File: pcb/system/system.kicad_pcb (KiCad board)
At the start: 2 copper layers, 32 parts, among them J1 Raspberry_Pi_4_GPIO, J2 Screw_Terminal_01x02, J3 Servo_1_Header, J4 Servo_2_Header, J5 Screw_Terminal_01x02, J6 Screw_Terminal_01x02, Q1 BS107A, Q2 BS107A, Q3 BS107A, Q4 BS107A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

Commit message: copium
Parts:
- added J7: Screw_Terminal_01x02, TerminalBlock_4Ucon:TerminalBlock_4Ucon_1x02_P3.50mm_Vertical, F.Cu at (169.8, 40.6)
- J1: moved to B.Cu
- Q5, Q6: footprint Package_TO_SOT_THT:TO-92L_Inline -> Package_TO_SOT_THT:TO-92L_HandSolder
- SW1: footprint Button_Switch_SMD:SW_DIP_SPSTx01_Slide_6.7x4.1mm_W6.73mm_P2.54mm_LowProfile_JPin -> Button_Switch_THT:SW_CuK_JS202011CQN_DPDT_Straight
- SW2: footprint Button_Switch_THT:SW_PUSH_6mm -> Button_Switch_THT:SW_PUSH_6mm_H4.3mm
- Sol1, Sol2, Sol3, Sol4: footprint Connector_PinSocket_2.54mm:PinSocket_1x03_P2.54mm_Vertical -> Connector_PinSocket_2.54mm:PinSocket_1x02_P2.54mm_Vertical
- moved SW2 144.0 mm to (232.1, 104.3), turned to 180 degrees
- moved Q2 103.5 mm to (189.3, 139.1), turned to 180 degrees
- moved Sol1 93.1 mm to (187.1, 125.5), turned to 180 degrees
- moved Q4 88.2 mm to (163.0, 139.2), turned to 180 degrees
- moved Sol2 83.5 mm to (169.9, 125.4), turned to 180 degrees
- moved Sol3 82.1 mm to (160.8, 125.3), turned to 180 degrees
- moved Q3 77.8 mm to (172.1, 139.2), turned to 180 degrees
- moved Sol4 77.2 mm to (178.8, 125.4), turned to 180 degrees
- moved R5 74.6 mm to (188.8, 50.0), turned to -90 degrees
- moved SW1 73.1 mm to (150.7, 72.8)
- moved D1 72.5 mm to (199.3, 55.4), turned to 90 degrees
- moved J2 70.9 mm to (227.0, 130.2), turned to 180 degrees
- moved D2 70.8 mm to (203.8, 55.4), turned to 90 degrees
- moved R7 66.1 mm to (184.8, 49.8), turned to -90 degrees
- moved J1 63.7 mm to (131.8, 55.2), turned to 180 degrees
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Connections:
- D1 pad 1: Net-(R1-Pad2) -> Net-(D1-Pad1)
- D2 pad 1: Net-(R2-Pad2) -> Net-(D2-Pad1)
- J1 pad 14: /Ground -> GND
- J1 pad 20: /Ground -> GND
- J1 pad 25: /Ground -> GND
- J1 pad 30: /Ground -> GND
- J1 pad 34: /Ground -> GND
- J1 pad 39: /Ground -> GND
- J1 pad 6: /Ground -> GND
- J1 pad 9: /Ground -> GND
- J2 pad 1: /Encoder_1_A -> /Encoder_1_B
- J2 pad 2: /Encoder_1_B -> /Encoder_1_A
- R1 pad 2: Net-(R1-Pad2) -> Net-(D1-Pad1)
- R2 pad 2: Net-(R2-Pad2) -> Net-(D2-Pad1)
- R3 pad 2: Net-(R1-Pad2) -> Net-(D1-Pad1)
- R4 pad 2: Net-(R2-Pad2) -> Net-(D2-Pad1)
- Reg1 pad 4: /Ground -> GND
- SW2 pad 1: Net-(R1-Pad1) -> Net-(U1-Pad13)
- U1 pad 13: unconnected-(U1-Pad13) -> Net-(U1-Pad13)
- U1 pad 22: Net-(R2-Pad2) -> unconnected-(U1-Pad22)
- U1 pad 23: Net-(R1-Pad2) -> unconnected-(U1-Pad23)
- U1 pad 7: unconnected-(U1-Pad7) -> Net-(D1-Pad1)
- U1 pad 8: unconnected-(U1-Pad8) -> Net-(D2-Pad1)
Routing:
- net GND: track 0.00 -> 336.4 mm
- net +8V: track 0.00 -> 173.2 mm
- net Net-(R1-Pad1): track 165.4 -> 57.0 mm
- net /GPIO_5: track 0.00 -> 107.0 mm
- net /GPIO_26: track 0.00 -> 106.8 mm
- net /GPIO_6: track 0.00 -> 105.1 mm
- net /GPIO_19: track 0.00 -> 104.7 mm
- net /3.3V: track 0.00 -> 61.8 mm
- net /Encoder_1_A: track 14.1 -> 75.8 mm
- net /Encoder_1_B: track 14.5 -> 70.7 mm
- net /Encoder_2_A: track 11.2 -> 65.5 mm
- net Net-(D1-Pad1): track 0.00 -> 52.2 mm
- net Net-(Q5-Pad1): track 0.00 -> 52.1 mm
- net /Encoder_2_B: track 11.2 -> 59.0 mm
- net /GPIO_13: track 0.00 -> 45.4 mm
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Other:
- board outline added: 142.4 x 129.3 mm

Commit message: still need to future proof pcb
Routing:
- net GND: track 336.4 -> 460.6 mm
- net Net-(R1-Pad1): track 57.0 -> 59.3 mm
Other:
- board size 142.4 x 129.3 mm -> 136.7 x 117.6 mm
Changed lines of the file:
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@@
       (xy 170.986486 44.081081)
     ) (layer "B.Cu") (width 0.2) (fill solid))
-  (gr_rect (start 105.7 34.9) (end 248.1 164.2) (layer "Edge.Cuts") (width 0.1) (fill none))
+  (gr_rect (start 112.9 34.3) (end 249.6 151.9) (layer "Edge.Cuts") (width 0.1) (fill none))
   (segment (start 147.7 99) (end 147.7 108.1) (width 1.3) (layer "F.Cu") (net 1))
   (segment (start 167.64 98) (end 168.58 98) (width 1.3) (layer "F.Cu") (net 1))
   (segment (start 168.66 57.44) (end 168.66 97.92) (width 1.3) (layer "F.Cu") (net 1))
   (segment (start 155.9225 98) (end 167.64 98) (width 1.3) (layer "F.Cu") (net 1))
+  (segment (start 193.3 141) (end 193.3 122) (width 0.5) (layer "F.Cu") (net 1))
   (segment (start 173.905 40.645) (end 174.5 41.24) (width 1.3) (layer "F.Cu") (net 1))
   (segment (start 156.5 99) (end 147.7 99) (width 1.3) (layer "F.Cu") (net 1))
@@
   (segment (start 149.0325 109.4325) (end 149.0325 109.4675) (width 1.3) (layer "F.Cu") (net 1))
   (segment (start 168.66 97.92) (end 168.58 98) (width 1.3) (layer "F.Cu") (net 1))
+  (segment (start 186.76 139.05) (end 186.76 140.76) (width 0.5) (layer "F.Cu") (net 1))
+  (segment (start 193.3 122) (end 169.4 98.1) (width 0.5) (layer "F.Cu") (net 1))
   (segment (start 174.5 41.24) (end 174.5 51.6) (width 1.3) (layer "F.Cu") (net 1))
-  (segment (start 152.725 54.83) (end 163.07 54.83) (width 0.5) (layer "F.Cu") (net 1))
+  (segment (start 152.725 54.83) (end 163.07 54.83) (width 0.7) (layer "F.Cu") (net 1))
+  (segment (start 186.76 140.76) (end 188.9 142.9) (width 0.5) (layer "F.Cu") (net 1))
   (segment (start 167.5 56.92) (end 167.5 97.86) (width 1.3) (layer "F.Cu") (net 1))
   (segment (start 156.3 98.8) (end 156.5 99) (width 1.3) (layer "F.Cu") (net 1))
+  (segment (start 175.3 51.8) (end 175.3 41.4) (width 0.5) (layer "F.Cu") (net 1))
+  (segment (start 169.4 57.7) (end 175.3 51.8) (width 0.5) (layer "F.Cu") (net 1))
   (segment (start 167.58 99) (end 168.58 98) (width 1.3) (layer "F.Cu") (net 1))
   (segment (start 149.0325 109.4675) (end 151.19 109.4675) (width 1.3) (layer "F.Cu") (net 1))
@@
   (segment (start 167.5 97.86) (end 167.64 98) (width 1.3) (layer "F.Cu") (net 1))
   (segment (start 199.272 47.764) (end 203.772 47.764) (width 0.5) (layer "F.Cu") (net 1))
+  (segment (start 169.4 98.1) (end 169.4 57.7) (width 0.5) (layer "F.Cu") (net 1))
   (segment (start 173.25 40.645) (end 173.905 40.645) (width 1.3) (layer "F.Cu") (net 1))
-  (segment (start 163.07 54.83) (end 173.25 44.65) (width 0.5) (layer "F.Cu") (net 1))
+  (segment (start 163.07 54.83) (end 173.25 44.65) (width 0.7) (layer "F.Cu") (net 1))
+  (segment (start 174.545 40.645) (end 173.25 40.645) (width 0.5) (layer "F.Cu") (net 1))
+  (segment (start 188.9 142.9) (end 191.4 142.9) (width 0.5) (layer "F.Cu") (net 1))
   (segment (start 147.7 108.1) (end 149.0325 109.4325) (width 1.3) (layer "F.Cu") (net 1))
+  (segment (start 175.3 41.4) (end 174.545 40.645) (width 0.5) (layer "F.Cu") (net 1))
   (segment (start 172.062 66.074) (end 172.062 70.574) (width 0.5) (layer "F.Cu") (net 1))
   (segment (start 173.25 40.645) (end 173.25 43.25) (width 1.3) (layer "F.Cu") (net 1))
   (segment (start 173.25 43.25) (end 173.25 51.17) (width 1.3) (layer "F.Cu") (net 1))
   (segment (start 173.25 51.17) (end 167.5 56.92) (width 1.3) (layer "F.Cu") (net 1))
+  (segment (start 191.4 142.9) (end 193.3 141) (width 0.5) (layer "F.Cu") (net 1))
   (segment (start 156.5 99) (end 167.58 99) (width 1.3) (layer "F.Cu") (net 1))
   (segment (start 174.5 51.6) (end 168.66 57.44) (width 1.3) (layer "F.Cu") (net 1))
@@
   (segment (start 169.56 139.2) (end 169.56 142.94) (width 0.5) (layer "B.Cu") (net 1))
   (segment (start 178.36 143.04) (end 178.3 143.1) (width 0.5) (layer "B.Cu") (net 1))
-  (segment (start 152.725 57.37) (end 144.33 57.37) (width 0.5) (layer "B.Cu") (net 1))
-  (segment (start 144.33 57.37) (end 141.4 60.3) (width 0.5) (layer "B.Cu") (net 1))
-  (segment (start 141.38 60.28) (end 134.34 60.28) (width 0.5) (layer "B.Cu") (net 1))
+  (segment (start 152.725 57.37) (end 144.33 57.37) (width 0.7) (layer "B.Cu") (net 1))
+  (segment (start 144.33 57.37) (end 141.4 60.3) (width 0.7) (layer "B.Cu") (net 1))
+  (segment (start 141.38 60.28) (end 134.34 60.28) (width 0.7) (layer "B.Cu") (net 1))
   (segment (start 220.76 49.96) (end 220.76 59.48) (width 0.5) (layer "B.Cu") (net 1))
   (segment (start 169.4 143.1) (end 178.3 143.1) (width 0.5) (layer "B.Cu") (net 1))
@@
   (segment (start 135 46.5) (end 131.8 49.7) (width 0.5) (layer "B.Cu") (net 4))
   (segment (start 150.6925 68.5075) (end 158.2 61) (width 0.5) (layer "B.Cu") (net 4))
-  (segment (start 152.725 59.91) (end 145.11 59.91) (width 0.5) (layer "F.Cu") (net 5))
-  (segment (start 142.94 57.74) (end 134.34 57.74) (width 0.5) (layer "F.Cu") (net 5))
-  (segment (start 145.11 59.91) (end 142.94 57.74) (width 0.5) (layer "F.Cu") (net 5))
+  (segment (start 152.725 59.91) (end 145.11 59.91) (width 0.7) (layer "F.Cu") (net 5))
+  (segment (start 142.94 57.74) (end 134.34 57.74) (width 0.7) (layer "F.Cu") (net 5))
+  (segment (start 145.11 59.91) (end 142.94 57.74) (width 0.7) (layer "F.Cu") (net 5))
   (segment (start 160.9 143.7) (end 161.73 142.87) (width 0.5) (layer "F.Cu") (net 25))
   (segment (start 131.8 90.76) (end 124.84 90.76) (width 0.5) (layer "F.Cu") (net 25))
@@
   (segment (start 159.8875 90.9125) (end 159 91.8) (width 0.5) (layer "B.Cu") (net 45))
   (segment (start 159 104.6225) (end 161.69 107.3125) (width 0.5) (layer "B.Cu") (net 45))
-  (segment (start 152.725 52.29) (end 158.105 52.29) (width 0.5) (layer "F.Cu") (net 46))
-  (segment (start 158.105 52.29) (end 169.75 40.645) (width 0.5) (layer "F.Cu") (net 46))
+  (segment (start 152.725 52.29) (end 158.105 52.29) (width 0.7) (layer "F.Cu") (net 46))
+  (segment (start 158.105 52.29) (end 169.75 40.645) (width 0.7) (layer "F.Cu") (net 46))
   (segment (start 169.4 106.6) (end 168.95 107.05) (width 1.3) (layer "B.Cu") (net 46))
   (segment (start 169.75 43.75) (end 169.75 42.95) (width 1.3) (layer "B.Cu") (net 46))
@@
   (segment (start 168 91.8) (end 170.5 94.3) (width 1.3) (layer "B.Cu") (net 46))
   (segment (start 166.9825 92.1825) (end 169.4 94.6) (width 1.3) (layer "B.Cu") (net 46))
-  (segment (start 188.772 49.974) (end 192.974 49.974) (width 0.5) (layer "F.Cu") (net 47))
+  (segment (start 191.626 49.974) (end 196.2 45.4) (width 0.5) (layer "F.Cu") (net 47))
   (segment (start 226.554 50.034) (end 236 59.48) (width 0.5) (layer "F.Cu") (net 47))
   (segment (start 211.072 50.034) (end 214.872 50.034) (width 0.5) (layer "F.Cu") (net 47))
   (segment (start 188.632 49.834) (end 188.772 49.974) (width 0.5) (layer "F.Cu") (net 47))
-  (segment (start 192.974 49.974) (end 194.8 51.8) (width 0.5) (layer "F.Cu") (net 47))
-  (segment (start 209.6 51.8) (end 211.4 50) (width 0.5) (layer "F.Cu") (net 47))
+  (segment (start 206.8 45.4) (end 211.4 50) (width 0.5) (layer "F.Cu") (net 47))
+  (segment (start 188.772 49.974) (end 191.626 49.974) (width 0.5) (layer "F.Cu") (net 47))
   (segment (start 214.872 50.034) (end 226.554 50.034) (width 0.5) (layer "F.Cu") (net 47))
+  (segment (start 196.2 45.4) (end 206.8 45.4) (width 0.5) (layer "F.Cu") (net 47))
   (segment (start 184.772 49.834) (end 188.632 49.834) (width 0.5) (layer "F.Cu") (net 47))
-  (segment (start 194.8 51.8) (end 209.6 51.8) (width 0.5) (layer "F.Cu") (net 47))
   (segment (start 206.912 83.474) (end 219.626 83.474) (width 0.5) (layer "F.Cu") (net 81))
   (segment (start 179.682 70.574) (end 188.772 61.484) (width 0.5) (layer "F.Cu") (net 81))

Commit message: i think the pcb is done
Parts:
- Sol1, Sol2, Sol3, Sol4: footprint Connector_PinSocket_2.54mm:PinSocket_1x02_P2.54mm_Vertical -> Connector_PinSocket_2.54mm:PinSocket_1x01_P2.54mm_Vertical
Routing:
- net /Servo_Left: track 36.1 -> 37.6 mm

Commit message: awe
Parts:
- added C1: 22pF, Capacitor_THT:CP_Radial_Tantal_D4.5mm_P2.50mm, F.Cu at (117.8, 48.6)
- added C2: 22pF, Capacitor_THT:CP_Radial_Tantal_D4.5mm_P2.50mm, F.Cu at (118.0, 40.0)
- added J10: Conn_02x08_Odd_Even, Connector_PinHeader_2.54mm:PinHeader_2x08_P2.54mm_Vertical, F.Cu at (109.3, 65.5)
- added J11: Conn_02x04_Odd_Even, Connector_PinHeader_2.54mm:PinHeader_2x04_P2.54mm_Vertical, F.Cu at (237.3, 42.3)
- added J12: Conn_02x04_Odd_Even, Connector_PinHeader_2.54mm:PinHeader_2x04_P2.54mm_Vertical, F.Cu at (243.9, 42.3)
- added J8: USB_A, Connector_USB:USB_A_Molex_105057_Vertical, F.Cu at (128.2, 46.7)
- added J9: Conn_02x08_Odd_Even, Connector_PinHeader_2.54mm:PinHeader_2x08_P2.54mm_Vertical, F.Cu at (115.9, 65.5)
- J1: footprint Connector_PinSocket_2.54mm:PinSocket_2x20_P2.54mm_Vertical -> Connector_PinHeader_2.54mm:PinHeader_2x20_P2.54mm_Vertical; moved to F.Cu
- R1, R2, R5, R7: value 1.2k -> 1.2kΩ
- R3, R4, R6, R8: value 110 -> 110Ω
- moved Reg1 16.4 mm to (141.8, 37.5)
- turned J1 to 0 degrees
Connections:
- J1 pad 14: GND -> /Ground
- J1 pad 20: GND -> /Ground
- J1 pad 25: GND -> /Ground
- J1 pad 30: GND -> /Ground
- J1 pad 34: GND -> /Ground
- J1 pad 39: GND -> /Ground
- J1 pad 6: GND -> /Ground
- J1 pad 9: GND -> /Ground
- Reg1 pad 5: /5V -> Net-(Reg1-Pad5)
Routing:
- net GND: track 460.6 -> 513.1 mm
- net +8V: track 173.2 -> 127.8 mm
- net /3.3V: track 61.8 -> 38.6 mm
- net /5V: track 19.3 -> 0.00 mm
- net Net-(Reg1-Pad5): track 0.00 -> 14.0 mm
- net Net-(C1-Pad1): track 0.00 -> 12.2 mm
- net Net-(C2-Pad1): track 0.00 -> 11.1 mm
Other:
- board size 136.7 x 117.6 mm -> 151.2 x 118.2 mm

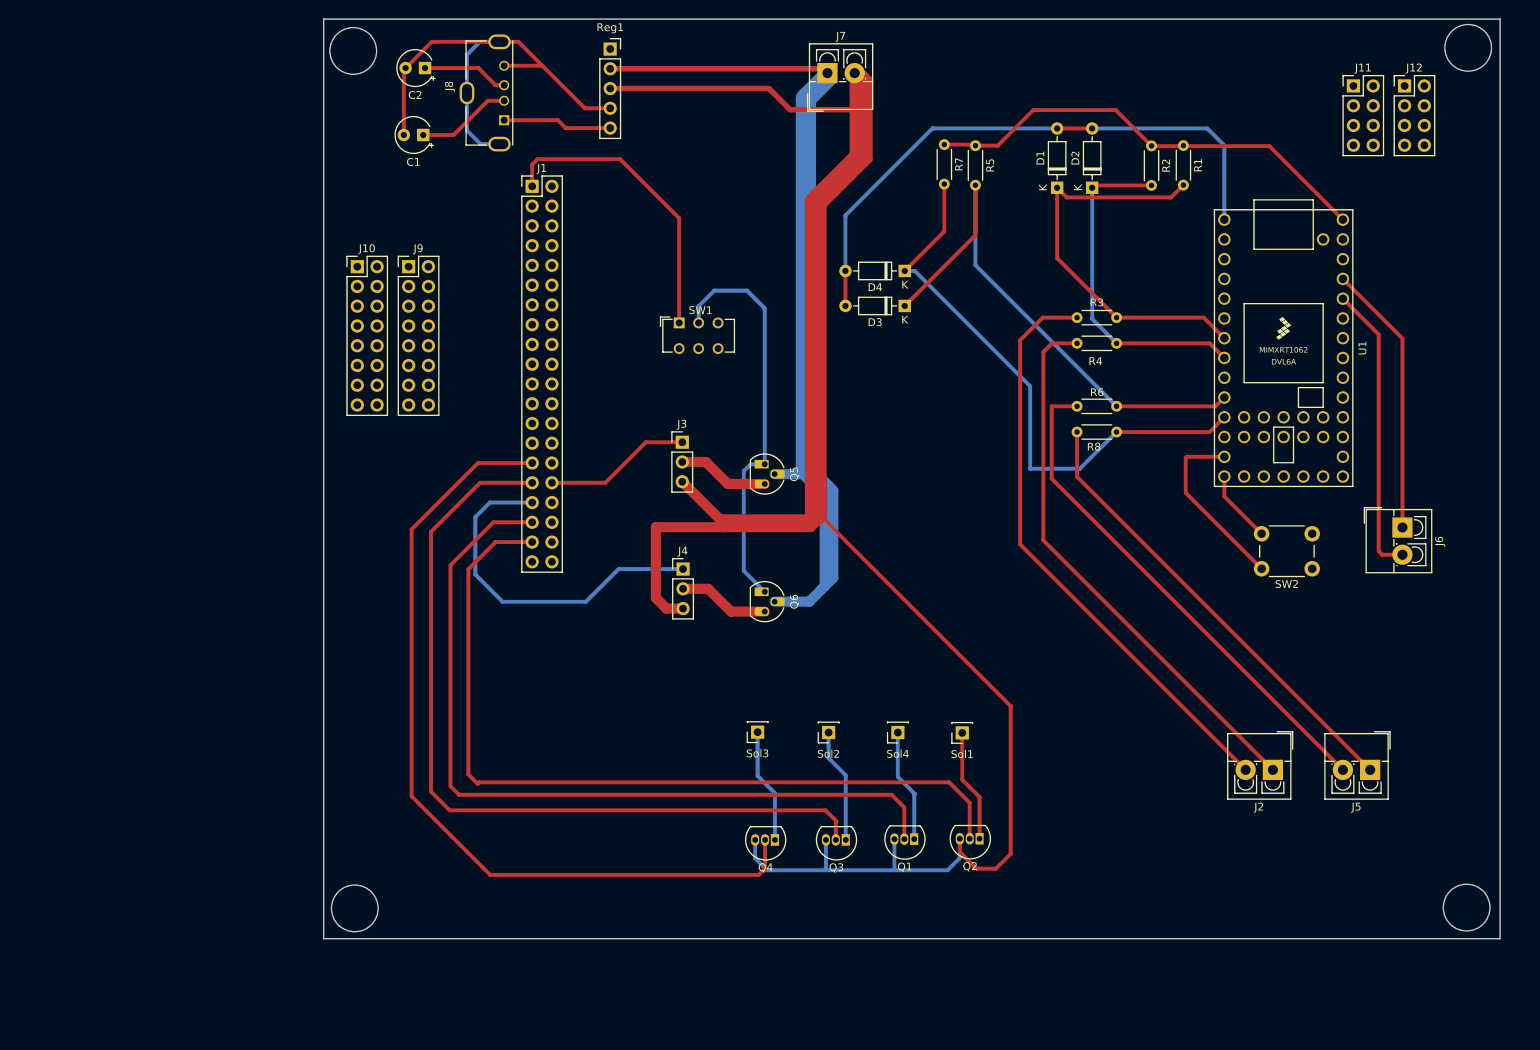
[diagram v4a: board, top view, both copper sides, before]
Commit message: thicker pcb traces
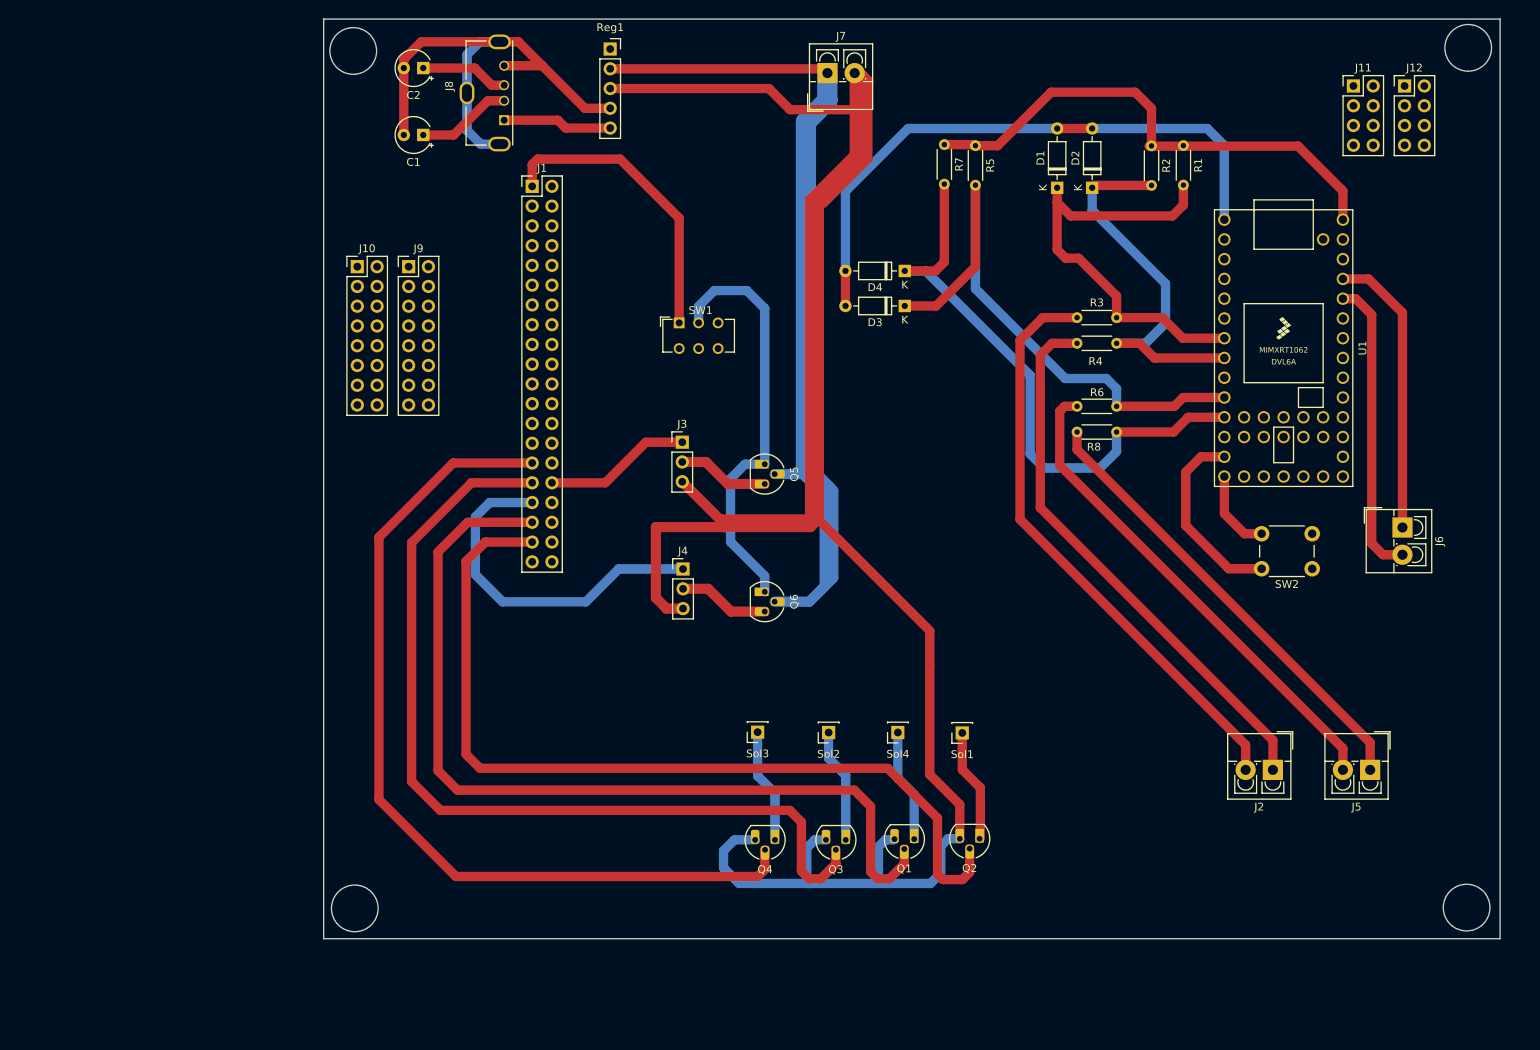
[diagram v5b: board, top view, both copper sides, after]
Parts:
- Q1, Q2, Q3, Q4: footprint Package_TO_SOT_THT:TO-92L_Inline -> Package_TO_SOT_THT:TO-92L_HandSolder
- moved C2 0.23 mm to (117.8, 40.0)
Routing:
- net GND: track 513.1 -> 478.4 mm
- net Net-(D3-Pad1): track 69.5 -> 81.7 mm
- net /GPIO_19: track 104.7 -> 115.1 mm
- net /GPIO_6: track 105.1 -> 115.4 mm
- net Net-(D4-Pad1): track 73.8 -> 83.3 mm
- net Net-(D2-Pad1): track 43.7 -> 51.1 mm
- net /GPIO_5: track 107.0 -> 114.0 mm
- net Net-(R1-Pad1): track 59.3 -> 66.2 mm
- net /GPIO_26: track 106.8 -> 113.4 mm
- net Net-(D1-Pad1): track 52.2 -> 55.9 mm
- net /Servo_Right: track 35.1 -> 37.1 mm
- net Net-(Q5-Pad1): track 52.1 -> 53.9 mm
- net /Encoder_2_A: track 65.5 -> 63.7 mm
- net Net-(SW2-Pad1): track 23.3 -> 24.7 mm
- net Net-(SW2-Pad2): track 9.33 -> 10.6 mm
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
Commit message: just making sure everything is pushed
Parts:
- removed J7: Screw_Terminal_01x02, TerminalBlock_4Ucon:TerminalBlock_4Ucon_1x02_P3.50mm_Vertical
- Q5, Q6: footprint Package_TO_SOT_THT:TO-92L_HandSolder -> Package_TO_SOT_THT:TO-92_HandSolder
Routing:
- net GND: track 478.4 -> 405.1 mm, vias 0 -> 1
- net +8V: track 128.4 -> 115.2 mm, vias 0 -> 1
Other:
- outline, holes or cut-outs redrawn
